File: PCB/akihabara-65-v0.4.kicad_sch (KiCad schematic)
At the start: 29 parts, among them J1 JST-SH, J2 SWD, Q1 2N7002, SW1 TS-1187A-B-A-B, U1 STM32F072C8Tx, U2 XC6206P332MR, Y1 16 MHz

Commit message: add gitignore
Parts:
- C8, C9: value 15pF -> 22pF
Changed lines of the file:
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@@
     (in_bom no) (on_board yes)
     (property "Reference" "C8" (id 0) (at 175.26 49.53 90))
-    (property "Value" "15pF" (id 1) (at 175.26 52.07 90))
+    (property "Value" "22pF" (id 1) (at 175.26 52.07 90))
     (property "Footprint" "Capacitor_SMD:C_0805_2012Metric" (id 2) (at 175.26 54.61 0)
       (effects (font (size 1.27 1.27)) hide)
@@
     (in_bom no) (on_board yes)
     (property "Reference" "C9" (id 0) (at 175.26 69.85 90))
-    (property "Value" "15pF" (id 1) (at 175.26 67.31 90))
+    (property "Value" "22pF" (id 1) (at 175.26 67.31 90))
     (property "Footprint" "Capacitor_SMD:C_0805_2012Metric" (id 2) (at 175.26 64.77 0)
       (effects (font (size 1.27 1.27)) hide)
@@
     )
     (path "/00000000-0000-0000-0000-000061caab83"
-      (reference "C8") (unit 1) (value "15pF") (footprint "Capacitor_SMD:C_0805_2012Metric")
+      (reference "C8") (unit 1) (value "22pF") (footprint "Capacitor_SMD:C_0805_2012Metric")
     )
     (path "/00000000-0000-0000-0000-000061cabe2a"
-      (reference "C9") (unit 1) (value "15pF") (footprint "Capacitor_SMD:C_0805_2012Metric")
+      (reference "C9") (unit 1) (value "22pF") (footprint "Capacitor_SMD:C_0805_2012Metric")
     )
     (path "/00000000-0000-0000-0000-0000620cc0a7"

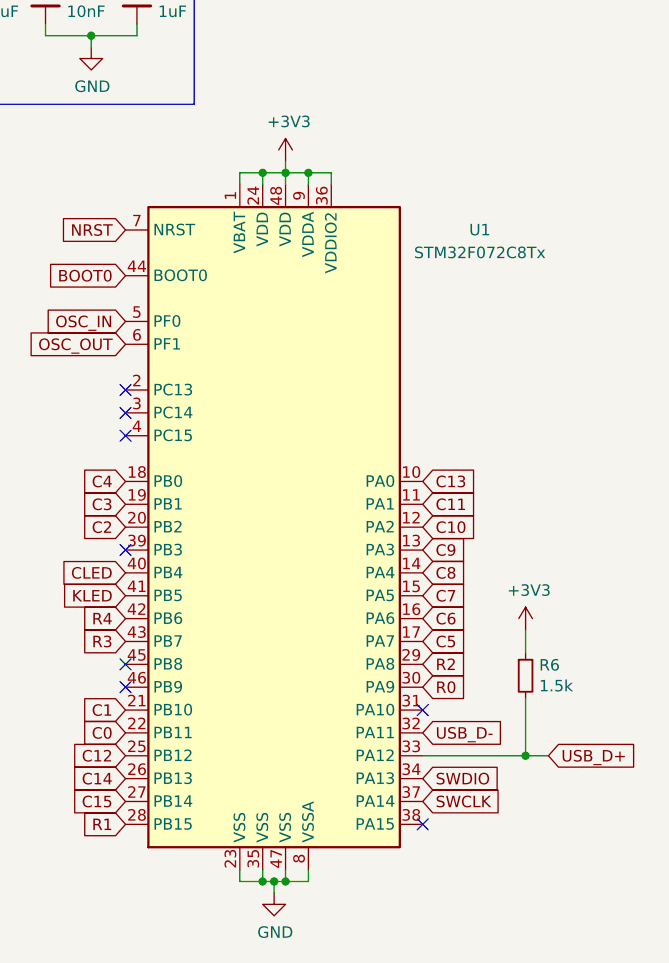
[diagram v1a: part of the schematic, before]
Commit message: PCB changes, readme, case files now added
- Changed MCU footprint from LQFP-48 to LQFP-48 + UFQFPN-48 dual footprint to combat MCU shortage
- PCB production files are for STM32F072CBUx; edit BOM, CPL, and paste layer if you want SMT assembly for an STM32F072CBTx
- STEP files and their associated technical drawings are now included for the case and plate
- Added more images, updated existing images
- Updated readme
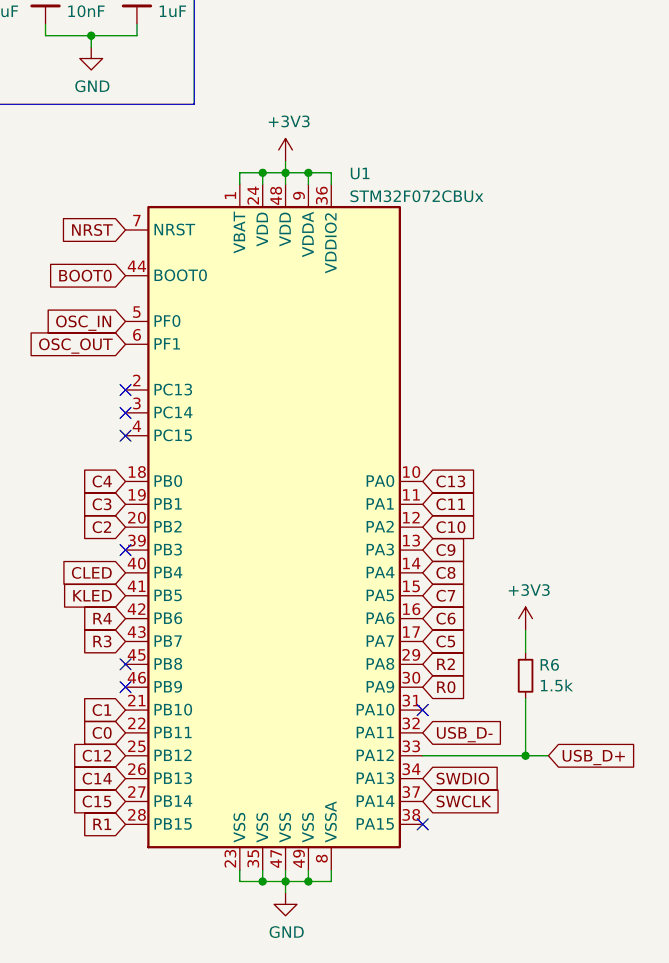
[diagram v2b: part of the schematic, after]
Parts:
- removed U1: STM32F072C8Tx, Package_QFP:LQFP-48_7x7mm_P0.5mm, symbol MCU_ST_STM32F0:STM32F072C8Tx
- added U1: STM32F072CBUx, Akihabara_Footprints:STM32_CxT_CxU_Hybrid, symbol MCU_ST_STM32F0:STM32F072CBUx
- C10, C11, C13, C7: LCSC 0805 -> C28323
- C8, C9: LCSC C1794 -> C1804
- J1: LCSC (none) -> C160404
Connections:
- net +3V3: now also U1.1 (VBAT), U1.24 (VDD), U1.36 (VDDIO2), U1.48 (VDD), U1.9 (VDDA)
- net BOOT0: now also U1.44 (BOOT0)
- net C0: now also U1.22 (PB11)
- net C1: now also U1.21 (PB10)
- net C10: now also U1.12 (PA2)
- net C11: now also U1.11 (PA1)
- net C12: now also U1.25 (PB12)
- net C13: now also U1.10 (PA0)
- net C14: now also U1.26 (PB13)
- net C15: now also U1.27 (PB14)
- net C2: now also U1.20 (PB2)
- net C3: now also U1.19 (PB1)
- net C4: now also U1.18 (PB0)
- net C5: now also U1.17 (PA7)
- net C6: now also U1.16 (PA6)
- net C7: now also U1.15 (PA5)
- net C8: now also U1.14 (PA4)
- net C9: now also U1.13 (PA3)
- net CLED: now also U1.40 (PB4)
- net GND: now also U1.23 (VSS), U1.35 (VSS), U1.47 (VSS), U1.49 (VSS), U1.8 (VSSA)
- net KLED: now also U1.41 (PB5)
- net NRST: now also U1.7 (NRST)
- net OSC_IN: now also U1.5 (PF0)
- net OSC_OUT: now also U1.6 (PF1)
- net R0: now also U1.30 (PA9)
- net R1: now also U1.28 (PB15)
- net R2: now also U1.29 (PA8)
- net R3: now also U1.43 (PB7)
- net R4: now also U1.42 (PB6)
- net SWCLK: now also U1.37 (PA14)
- net SWDIO: now also U1.34 (PA13)
- net USB_D+: now also U1.33 (PA12)
- net USB_D-: now also U1.32 (PA11)
